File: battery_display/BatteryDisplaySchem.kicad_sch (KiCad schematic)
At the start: 2 parts, among them U1 E2206KS0E1

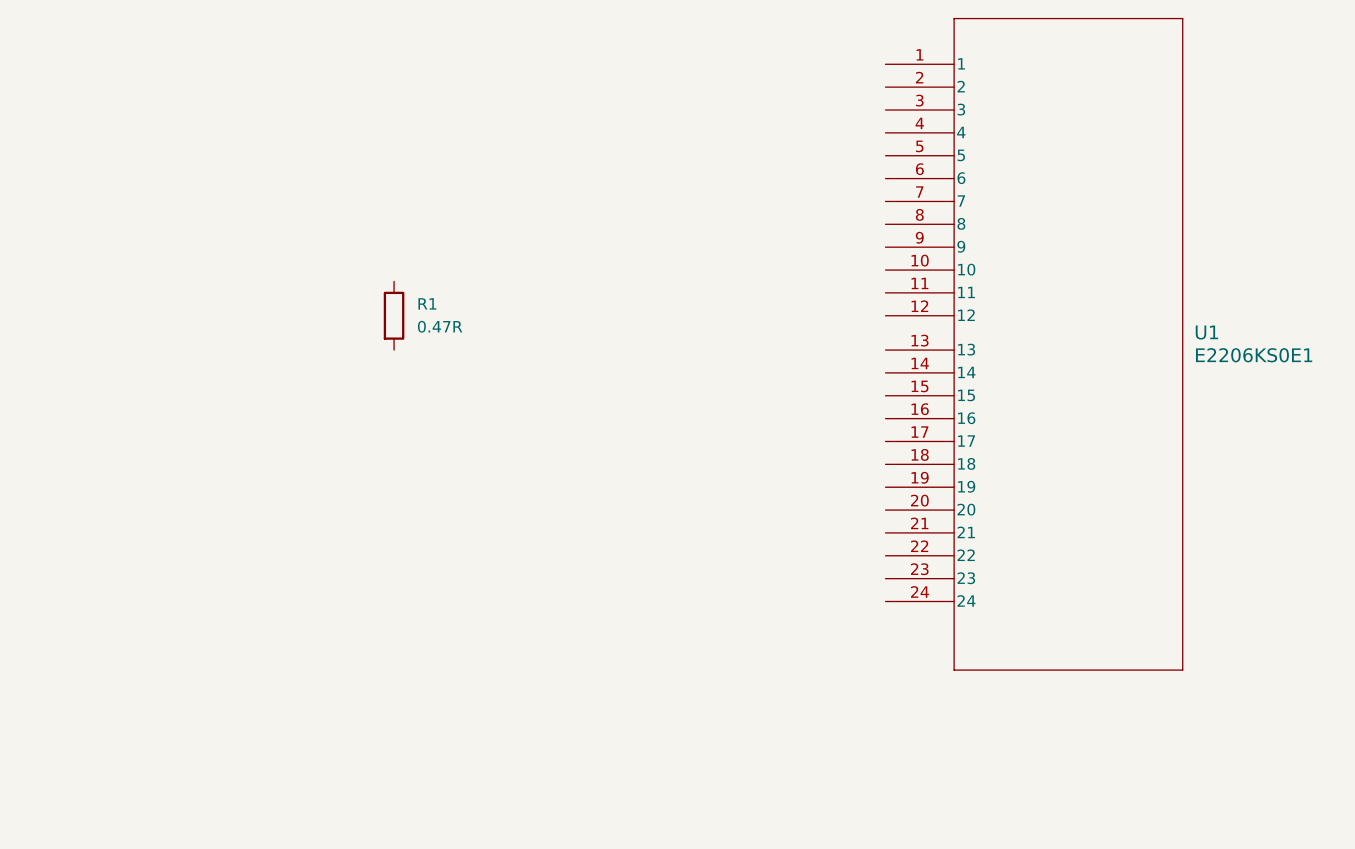
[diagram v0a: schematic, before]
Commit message: Update BatteryDisplaySchem.kicad_sch
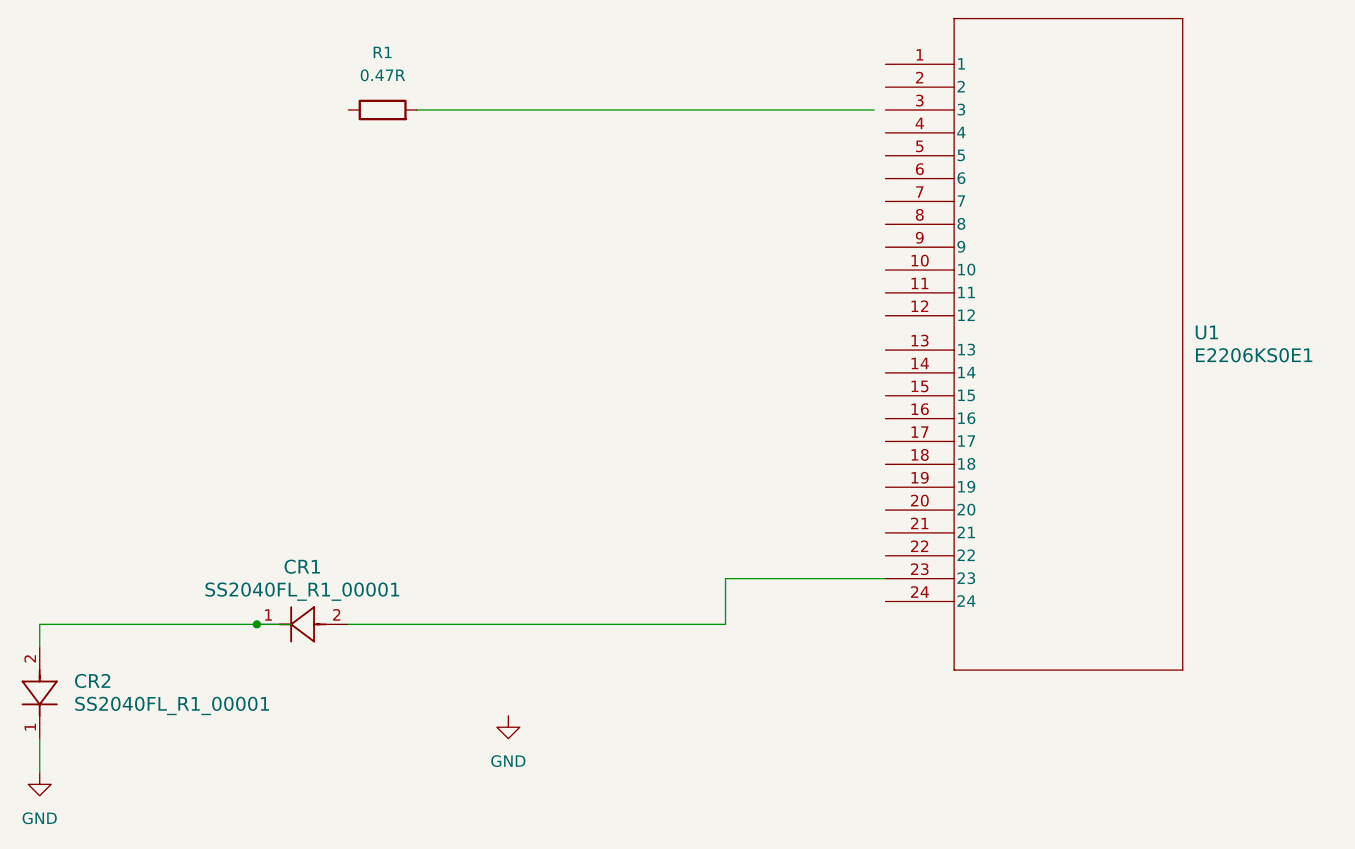
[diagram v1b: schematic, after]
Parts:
- added CR1, CR2: SS2040FL_R1_00001, CR_R1_00001_PNJ, symbol rsx_diodes:SS2040FL_R1_00001
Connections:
- net at U1.23: now also CR1.2
- new net: CR1.1, CR2.2
- new net GND: CR2.1
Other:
- moved on the sheet: R1
